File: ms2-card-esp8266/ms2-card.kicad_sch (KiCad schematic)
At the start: 58 parts, among them J1 Schaltregler, J10 MicroSD_SPI_CD, J11 Conn_01x06, J2 ESP Prog, J20 Smartcard Connector, J21 PogoPin, J22 Card Edge, J23 Conn_01x04, J30 USB_B_Micro, J31 Power Select, J32 Conn_01x03, Q1 MMBT3904, Q2 MMBT3904, SW1 RESET, U1 ESP-12F, U2 FM24C64B, U20 BL1551B, U3 BL1551B, U30 CP2102N-Axx-xQFN24, U4 BL1551B, U6 AMS1117-3.3

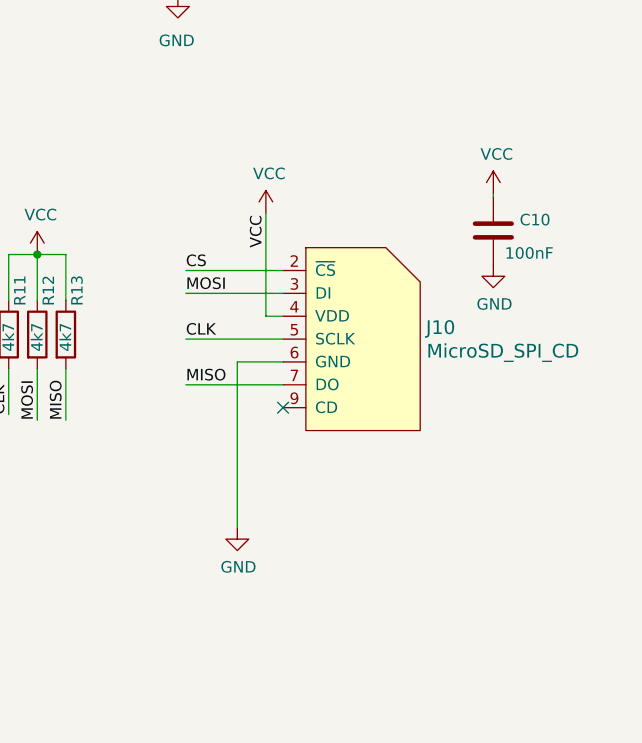
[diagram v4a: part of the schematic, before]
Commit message: fix SD CARD DRC check
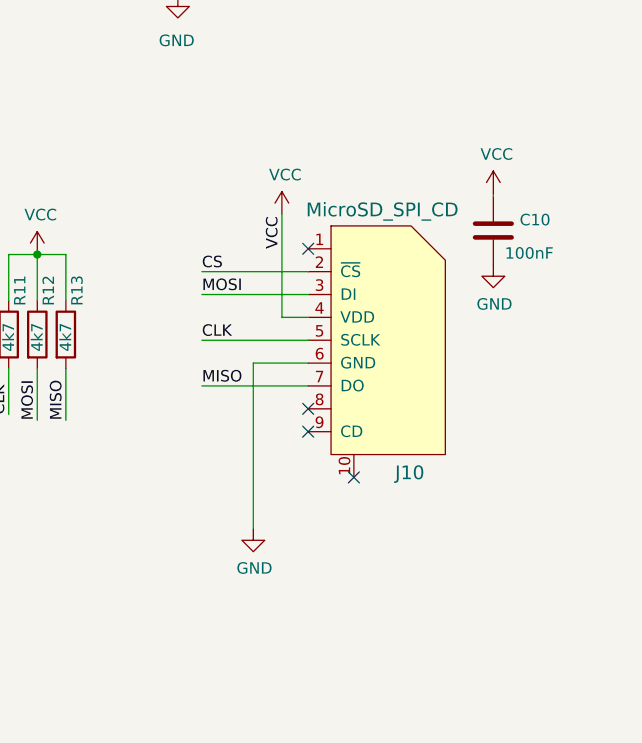
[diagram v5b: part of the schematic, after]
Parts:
- removed J10: MicroSD_SPI_CD, w_conn_misc:GCT-MEM2055-00-190-01-A, symbol microsd_spi_cd:MicroSD_SPI_CD
- added J10: MicroSD_SPI_CD, sd-card-conn:GCT-MEM2055-00-190-01-A, symbol microsd_spi_cd_new:MicroSD_SPI_CD
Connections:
- net CLK: now also J10.5 (SCLK)
- net CS: now also J10.2 (~{CS})
- net GND: now also J10.6 (GND)
- net MISO: now also J10.7 (DO)
- net MOSI: now also J10.3 (DI)
- net VCC: now also J10.4 (VDD)
- no-connect marks 23 -> 26
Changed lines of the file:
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@@
   (no_connect (at 222.25 63.754))
   (no_connect (at 86.614 115.824))
-  (no_connect (at 246.634 130.175))
+  (no_connect (at 249.428 130.302))
   (no_connect (at 273.812 56.134))
+  (no_connect (at 254.508 137.922))
   (no_connect (at 39.37 152.4))
   (no_connect (at 263.652 51.054))
   (no_connect (at 222.25 53.594))
   (no_connect (at 86.614 108.204))
+  (no_connect (at 249.428 112.522))
   (no_connect (at 86.614 113.284))
   (no_connect (at 222.25 66.294))
@@
   (no_connect (at 222.25 48.514))
   (no_connect (at 222.25 56.134))
+  (no_connect (at 249.428 132.842))
   (no_connect (at 39.37 147.32))
   (wire (pts (xy 91.059 39.116) (xy 100.584 39.116))
@@
     (stroke (width 0) (type default) (color 0 0 0 0))
   )
-  (wire (pts (xy 246.634 117.475) (xy 235.839 117.475))
+  (wire (pts (xy 249.428 117.602) (xy 237.617 117.602))
     (stroke (width 0) (type default) (color 0 0 0 0))
   )
@@
     (stroke (width 0) (type default) (color 0 0 0 0))
   )
-  (wire (pts (xy 235.839 127.635) (xy 246.634 127.635))
+  (wire (pts (xy 237.617 127.762) (xy 249.428 127.762))
     (stroke (width 0) (type default) (color 0 0 0 0))
   )
@@
     (stroke (width 0) (type default) (color 0 0 0 0))
   )
-  (wire (pts (xy 246.634 120.015) (xy 244.729 120.015))
+  (wire (pts (xy 249.428 120.142) (xy 246.507 120.142))
     (stroke (width 0) (type default) (color 0 0 0 0))
   )
@@
     (stroke (width 0) (type default) (color 0 0 0 0))
   )
-  (wire (pts (xy 241.554 125.095) (xy 241.554 143.51))
+  (wire (pts (xy 243.332 125.222) (xy 243.332 143.637))
     (stroke (width 0) (type default) (color 0 0 0 0))
   )
@@
     (stroke (width 0) (type default) (color 0 0 0 0))
   )
-  (wire (pts (xy 244.729 120.015) (xy 244.729 108.585))
+  (wire (pts (xy 246.507 120.142) (xy 246.507 108.712))
     (stroke (width 0) (type default) (color 0 0 0 0))
   )
@@
     (stroke (width 0) (type default) (color 0 0 0 0))
   )
-  (wire (pts (xy 246.634 114.935) (xy 235.839 114.935))
+  (wire (pts (xy 249.428 115.062) (xy 237.617 115.062))
     (stroke (width 0) (type default) (color 0 0 0 0))
   )
@@
     (stroke (width 0) (type default) (color 0 0 0 0))
   )
-  (wire (pts (xy 246.634 122.555) (xy 235.839 122.555))
+  (wire (pts (xy 249.428 122.682) (xy 237.617 122.682))
     (stroke (width 0) (type default) (color 0 0 0 0))
   )
@@
     (stroke (width 0) (type default) (color 0 0 0 0))
   )
-  (wire (pts (xy 246.634 125.095) (xy 241.554 125.095))
+  (wire (pts (xy 249.428 125.222) (xy 243.332 125.222))
     (stroke (width 0) (type default) (color 0 0 0 0))
   )
@@
     (effects (font (size 1.27 1.27)) (justify left bottom))
   )
-  (label "CS" (at 235.839 114.935 0)
+  (label "CS" (at 237.617 115.062 0)
     (effects (font (size 1.27 1.27)) (justify left bottom))
   )
@@
     (effects (font (size 1.27 1.27)) (justify left bottom))
   )
-  (label "CLK" (at 235.839 122.555 0)
+  (label "CLK" (at 237.617 122.682 0)
     (effects (font (size 1.27 1.27)) (justify left bottom))
   )
@@
     (effects (font (size 1.27 1.27)) (justify right bottom))
   )
-  (label "VCC" (at 244.729 112.395 90)
+  (label "VCC" (at 246.507 112.522 90)
     (effects (font (size 1.27 1.27)) (justify left bottom))
   )
@@
     (effects (font (size 1.27 1.27)) (justify left bottom))
   )
-  (label "MOSI" (at 235.839 117.475 0)
+  (label "MOSI" (at 237.617 117.602 0)
     (effects (font (size 1.27 1.27)) (justify left bottom))
   )
@@
     (effects (font (size 1.27 1.27)) (justify right bottom))
   )
-  (label "MISO" (at 235.839 127.635 0)
+  (label "MISO" (at 237.617 127.762 0)
     (effects (font (size 1.27 1.27)) (justify left bottom))
   )
@@
     (pin "4")
   )
-  (symbol (lib_id "power:GND") (at 241.554 143.51 0) (unit 1)
+  (symbol (lib_id "power:GND") (at 243.332 143.637 0) (unit 1)
     (in_bom yes) (on_board yes)
-    (property "Reference" "#PWR0107" (id 0) (at 241.554 149.86 0)
+    (property "Reference" "#PWR0107" (id 0) (at 243.332 149.987 0)
       (effects (font (size 1.27 1.27)) hide)
     )
-    (property "Value" "GND" (id 1) (at 241.681 147.9042 0))
-    (property "Footprint" "" (id 2) (at 241.554 143.51 0)
+    (property "Value" "GND" (id 1) (at 243.459 148.0312 0))
+    (property "Footprint" "" (id 2) (at 243.332 143.637 0)
       (effects (font (size 1.27 1.27)) hide)
     )
-    (property "Datasheet" "" (id 3) (at 241.554 143.51 0)
+    (property "Datasheet" "" (id 3) (at 243.332 143.637 0)
       (effects (font (size 1.27 1.27)) hide)
     )
     (pin "1")
   )
-  (symbol (lib_id "power:VCC") (at 244.729 108.585 0) (unit 1)
+  (symbol (lib_id "power:VCC") (at 246.507 108.712 0) (unit 1)
     (in_bom yes) (on_board yes)
-    (property "Reference" "#PWR0108" (id 0) (at 244.729 112.395 0)
+    (property "Reference" "#PWR0108" (id 0) (at 246.507 112.522 0)
       (effects (font (size 1.27 1.27)) hide)
     )
-    (property "Value" "VCC" (id 1) (at 245.11 104.1908 0))
-    (property "Footprint" "" (id 2) (at 244.729 108.585 0)
+    (property "Value" "VCC" (id 1) (at 246.888 104.3178 0))
+    (property "Footprint" "" (id 2) (at 246.507 108.712 0)
       (effects (font (size 1.27 1.27)) hide)
     )
-    (property "Datasheet" "" (id 3) (at 244.729 108.585 0)
+    (property "Datasheet" "" (id 3) (at 246.507 108.712 0)
       (effects (font (size 1.27 1.27)) hide)
     )
@@
     (pin "3")
   )
-  (symbol (lib_id "microsd_spi_cd:MicroSD_SPI_CD") (at 255.524 122.555 0) (mirror y) (unit 1)
-    (in_bom yes) (on_board yes)
-    (property "Reference" "J10" (id 0) (at 262.509 121.285 0)
-      (effects (font (size 1.524 1.524)) (justify right))
-    )
-    (property "Value" "MicroSD_SPI_CD" (id 1) (at 262.5852 123.9012 0)
-      (effects (font (size 1.524 1.524)) (justify right))
-    )
-    (property "Footprint" "w_conn_misc:GCT-MEM2055-00-190-01-A" (id 2) (at 259.334 122.555 0)
-      (effects (font (size 1.524 1.524)) hide)
-    )
-    (property "Datasheet" "" (id 3) (at 259.334 122.555 0)
-      (effects (font (size 1.524 1.524)))
-    )
-    (property "LCSC" "C2889258" (id 4) (at 255.524 122.555 0)
-      (effects (font (size 1.27 1.27)) hide)
-    )
-    (pin "2")
-    (pin "3")
-    (pin "4")
-    (pin "5")
-    (pin "6")
-    (pin "7")
-    (pin "9")
-  )
   (symbol (lib_id "Connector_Generic:Conn_01x04") (at 19.304 50.546 180) (unit 1)
     (in_bom yes) (on_board yes)
@@
     (pin "1")
   )
+  (symbol (lib_id "microsd_spi_cd_new:MicroSD_SPI_CD") (at 258.318 122.682 0) (mirror y) (unit 1)
+    (in_bom yes) (on_board yes)
+    (property "Reference" "J10" (id 0) (at 259.08 137.414 0)
+      (effects (font (size 1.524 1.524)) (justify right))
+    )
+    (property "Value" "MicroSD_SPI_CD" (id 1) (at 249.174 108.204 0)
+      (effects (font (size 1.524 1.524)) (justify right))
+    )
+    (property "Footprint" "sd-card-conn:GCT-MEM2055-00-190-01-A" (id 2) (at 262.128 122.682 0)
+      (effects (font (size 1.524 1.524)) hide)
+    )
+    (property "Datasheet" "" (id 3) (at 262.128 122.682 0)
+      (effects (font (size 1.524 1.524)))
+    )
+    (property "LCSC" "C2889258" (id 4) (at 265.303 126.1092 0)
+      (effects (font (size 1.27 1.27)) (justify right) hide)
+    )
+    (pin "1")
+    (pin "10")
+    (pin "2")
+    (pin "3")
+    (pin "4")
+    (pin "5")
+    (pin "6")
+    (pin "7")
+    (pin "8")
+    (pin "9")
+  )
   (symbol (lib_id "power:GND") (at 234.95 84.328 0) (unit 1)
     (in_bom yes) (on_board yes)
@@
       (reference "J2") (unit 1) (value "ESP Prog") (footprint "Connector_PinHeader_2.54mm:PinHeader_1x02_P2.54mm_Vertical")
     )
-    (path "/00000000-0000-0000-0000-0000628636b3"
-      (reference "J10") (unit 1) (value "MicroSD_SPI_CD") (footprint "w_conn_misc:GCT-MEM2055-00-190-01-A")
+    (path "/ebb4483f-f4e3-428b-be91-682a1e999981"
+      (reference "J10") (unit 1) (value "MicroSD_SPI_CD") (footprint "sd-card-conn:GCT-MEM2055-00-190-01-A")
     )
     (path "/88080054-9bba-4f0e-aaf1-9272cbd30b3b"

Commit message: minor changes
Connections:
- net VBUS: now also C5.1, J1.3 (Pin_3), U6.3 (VI); no longer J31.3 (Pin_3)
- net VCC: now also J31.2 (Pin_2); no longer C6.1, C7.1, U6.2 (VO)
- removed net +5V: C5.1, J1.3 (Pin_3), J31.2 (Pin_2), U6.3 (VI)
- new net +3V3: C6.1, C7.1, J31.3 (Pin_3), U6.2 (VO)
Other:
- moved on the sheet: J1

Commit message: wip
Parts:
- removed D2: LED, LED_SMD:LED_0603_1608Metric, symbol Device:LED
- removed R7: 330, Resistor_SMD:R_0603_1608Metric, symbol Device:R
- R3: value 0 -> 220K; LCSC C21189 -> C22961
- R4: value 0 -> 100K; LCSC C21189 -> C25803
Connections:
- net LED is gone; now on net Card: U1.4 (GPIO16)
- net CSCL: now also R3.1; no longer R3.2
- net CSDA: no longer R4.2
- net Card: no longer U1.14 (SCLK)
- net GND: now also R4.1
- net at U1.11 (GPIO9): no longer R4.1
- net at U1.12 (GPIO10): no longer R3.1
- net at U1.2 (ADC): now also R3.2, R4.2
- no-connect marks 26 -> 28

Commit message: add 3D pic
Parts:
- added C8: 1uF, Capacitor_SMD:C_0603_1608Metric, symbol Device:C
- added Q3: MMBT5401, Package_TO_SOT_SMD:SOT-23, symbol Transistor_BJT:MMBT3906
- R4: value 100K -> 4k7; LCSC C25803 -> C23162
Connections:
- net CSCL: now also R4.1; no longer R3.1
- net GND: now also R3.1, C8.2; no longer R4.1
- net VCC: now also Q3.2 (E)
- net ADC: now reaches R3.2, U1.2 (ADC)
- net ADC: now also C8.1, Q3.3 (C); no longer R4.2
- new net: Q3.1 (B), R4.2
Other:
- moved on the sheet: C1, J2, R3
